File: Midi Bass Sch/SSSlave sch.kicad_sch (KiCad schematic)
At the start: 10 parts, among them J4 A SLAVE ISCP, U3 PIC16F1789

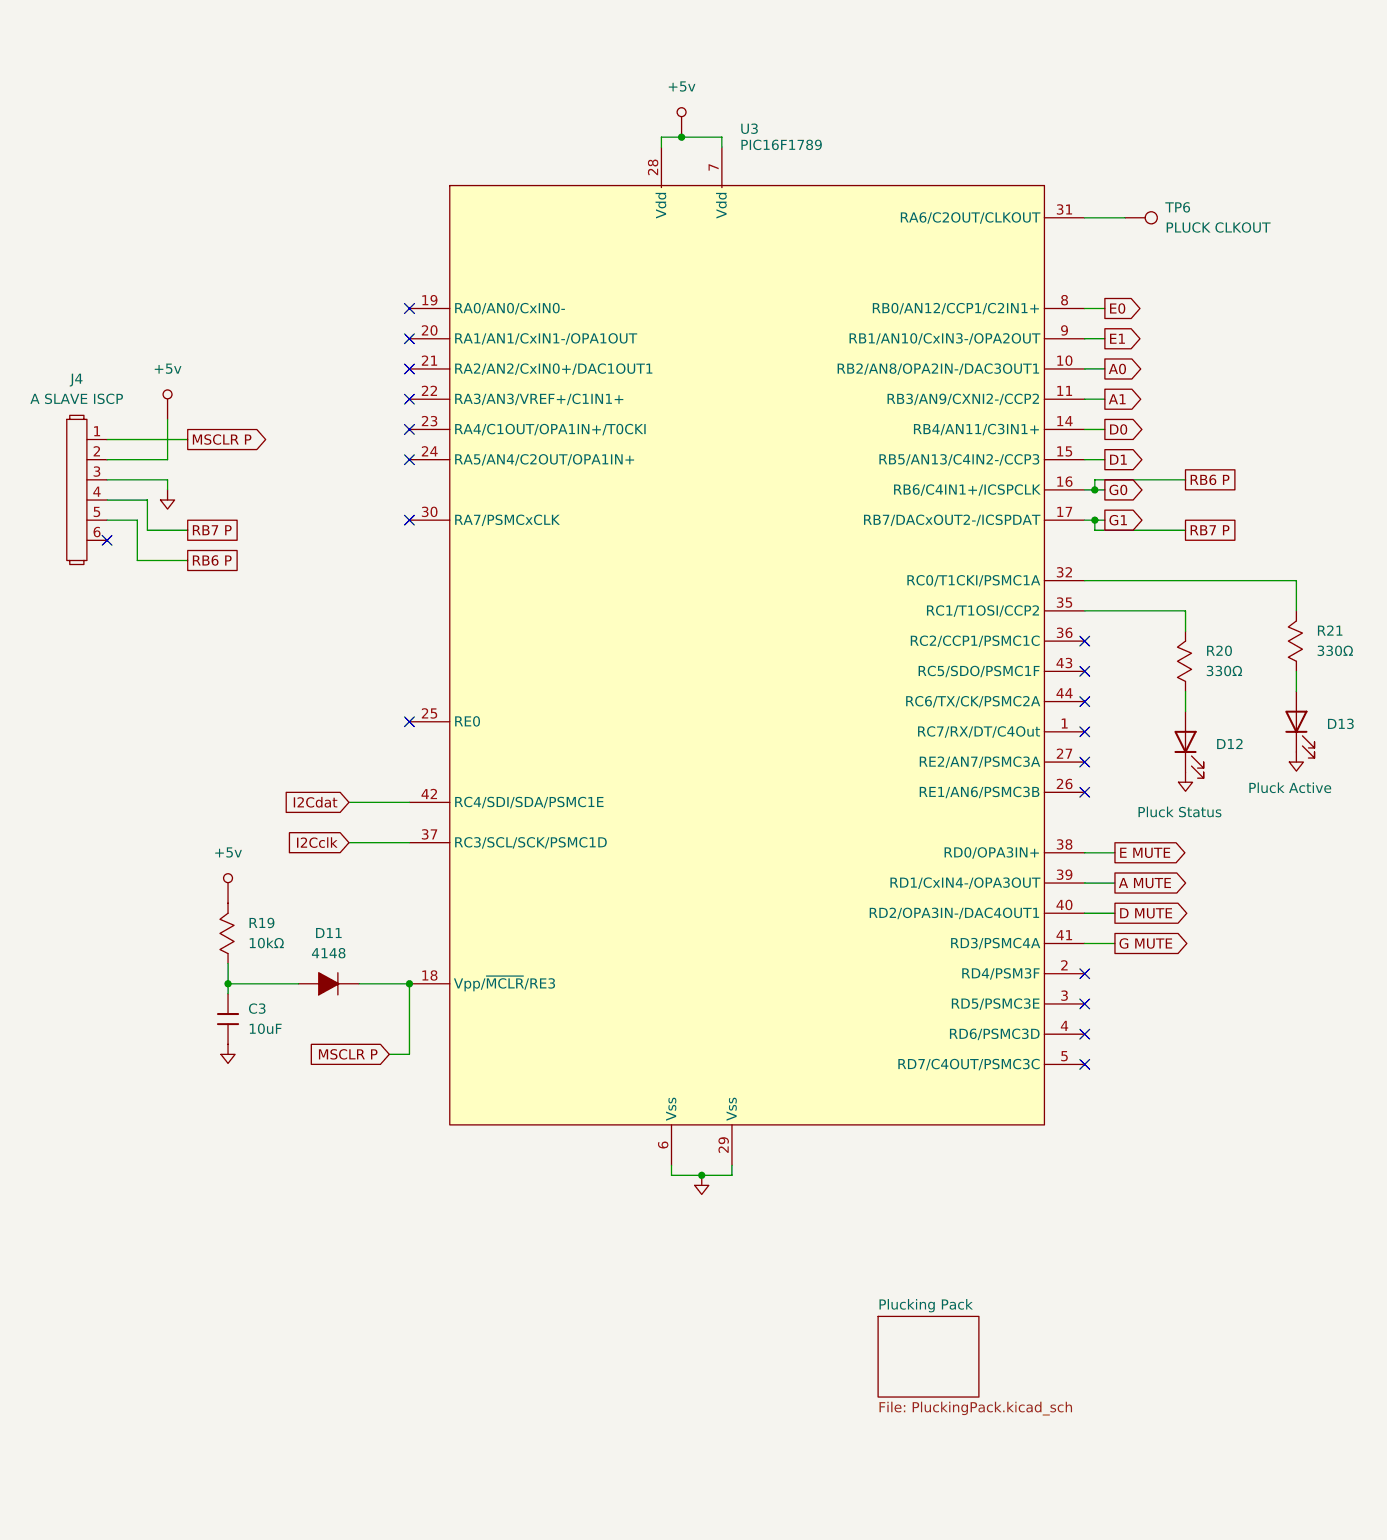
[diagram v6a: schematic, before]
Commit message: updated schematic to reflect code
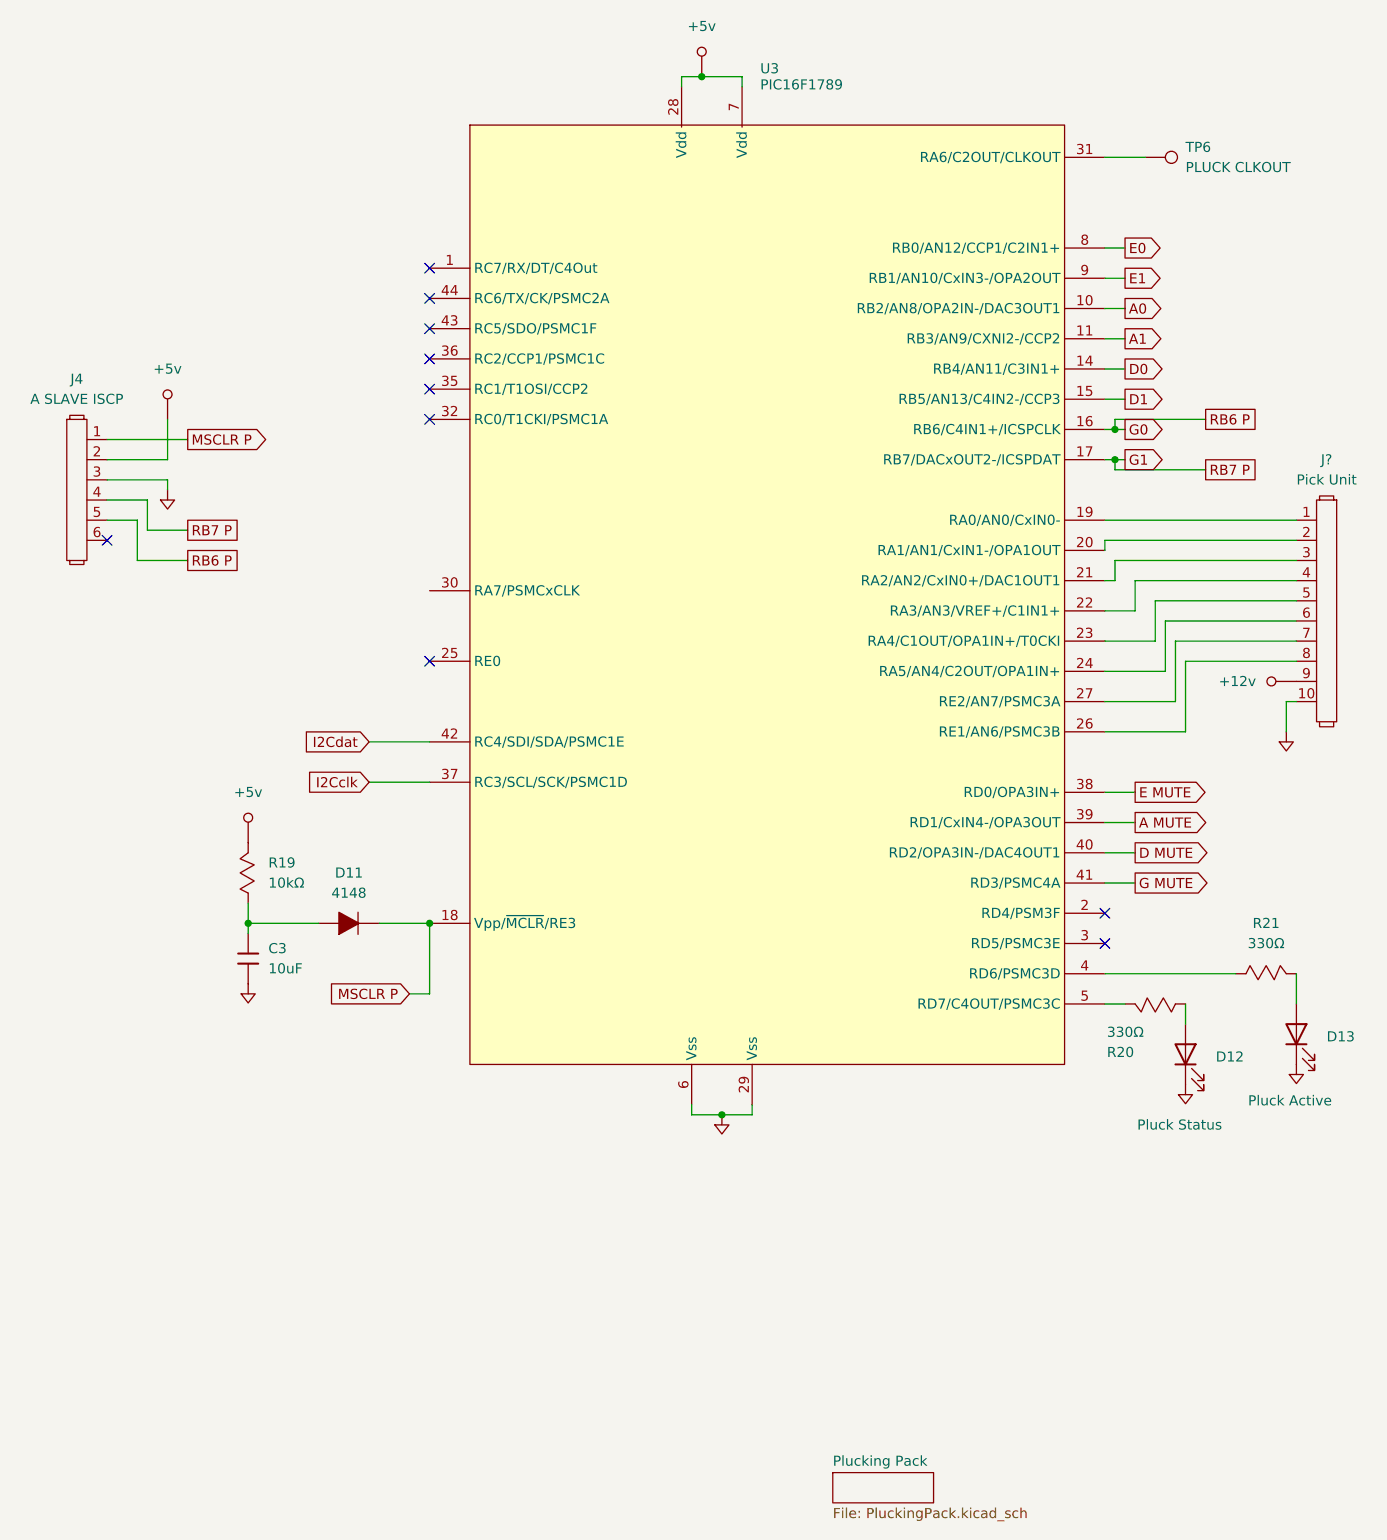
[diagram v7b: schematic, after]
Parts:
- added J?: Pick Unit, symbol Owen's Symbols:Header_1x10
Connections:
- net GND: now also J?.10
- net at R21.1: now also U3.4 (RD6/PSMC3D); no longer D13.2 (A)
- net at R21.2: now also D13.2 (A); no longer U3.32 (RC0/T1CKI/PSMC1A)
- net at U3.35 (RC1/T1OSI/CCP2): now also J?.2; no longer R20.2
- net at U3.1 (RC7/RX/DT/C4Out): now also J?.8
- net at U3.36 (RC2/CCP1/PSMC1C): now also J?.3
- net at U3.37 (RC3/SCL/SCK/PSMC1D): now also J?.4
- net at U3.42 (RC4/SDI/SDA/PSMC1E): now also J?.5
- net at U3.43 (RC5/SDO/PSMC1F): now also J?.6
- net at U3.44 (RC6/TX/CK/PSMC2A): now also J?.7
- net at U3.5 (RD7/C4OUT/PSMC3C): now also R20.2
- new net: J?.1, U3.32 (RC0/T1CKI/PSMC1A)
- new net +12v: J?.9
- no-connect marks 19 -> 10
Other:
- moved on the sheet: C3, D11, D12, D13, R19, R20, R21, TP6, U3

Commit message: working on troubleshooting section of report
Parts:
- gave numbers to parts that had none: 1
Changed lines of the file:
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@@
 		(dnp no)
 		(fields_autoplaced yes)
-		(property "Reference" "#PWR0343"
+		(property "Reference" "#PWR038"
 			(at 182.9816 91.7956 0)
 			(effects
@@
 			(project ""
 				(path "/06818073-fb22-48ee-acc5-6dedd827034e/673444b1-2638-4f61-b545-e7cdf999c0e0"
-					(reference "#PWR0343")
+					(reference "#PWR038")
 					(unit 1)
 				)
@@
 		(dnp no)
 		(fields_autoplaced yes)
-		(property "Reference" "#PWR038"
+		(property "Reference" "#PWR040"
 			(at 187.96 143.51 0)
 			(effects
@@
 			(project "Midi Bass Sch"
 				(path "/06818073-fb22-48ee-acc5-6dedd827034e/673444b1-2638-4f61-b545-e7cdf999c0e0"
-					(reference "#PWR038")
+					(reference "#PWR040")
 					(unit 1)
 				)
@@
 		(on_board yes)
 		(dnp no)
-		(property "Reference" "J?"
+		(property "Reference" "J5"
 			(at 191.77 68.58 0)
 			(effects
@@
 			(project ""
 				(path "/06818073-fb22-48ee-acc5-6dedd827034e/673444b1-2638-4f61-b545-e7cdf999c0e0"
-					(reference "J?")
+					(reference "J5")
 					(unit 1)
 				)
@@
 		(dnp no)
 		(fields_autoplaced yes)
-		(property "Reference" "#PWR0342"
+		(property "Reference" "#PWR039"
 			(at 186.69 101.6 0)
 			(effects
@@
 			(project "Midi Bass Sch"
 				(path "/06818073-fb22-48ee-acc5-6dedd827034e/673444b1-2638-4f61-b545-e7cdf999c0e0"
-					(reference "#PWR0342")
-					(unit 1)
-				)
+					(reference "#PWR039")
+					(unit 1)
+				)
